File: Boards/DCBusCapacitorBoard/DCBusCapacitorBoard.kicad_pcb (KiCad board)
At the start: 4 copper layers, 89 x 85 mm, 16 parts

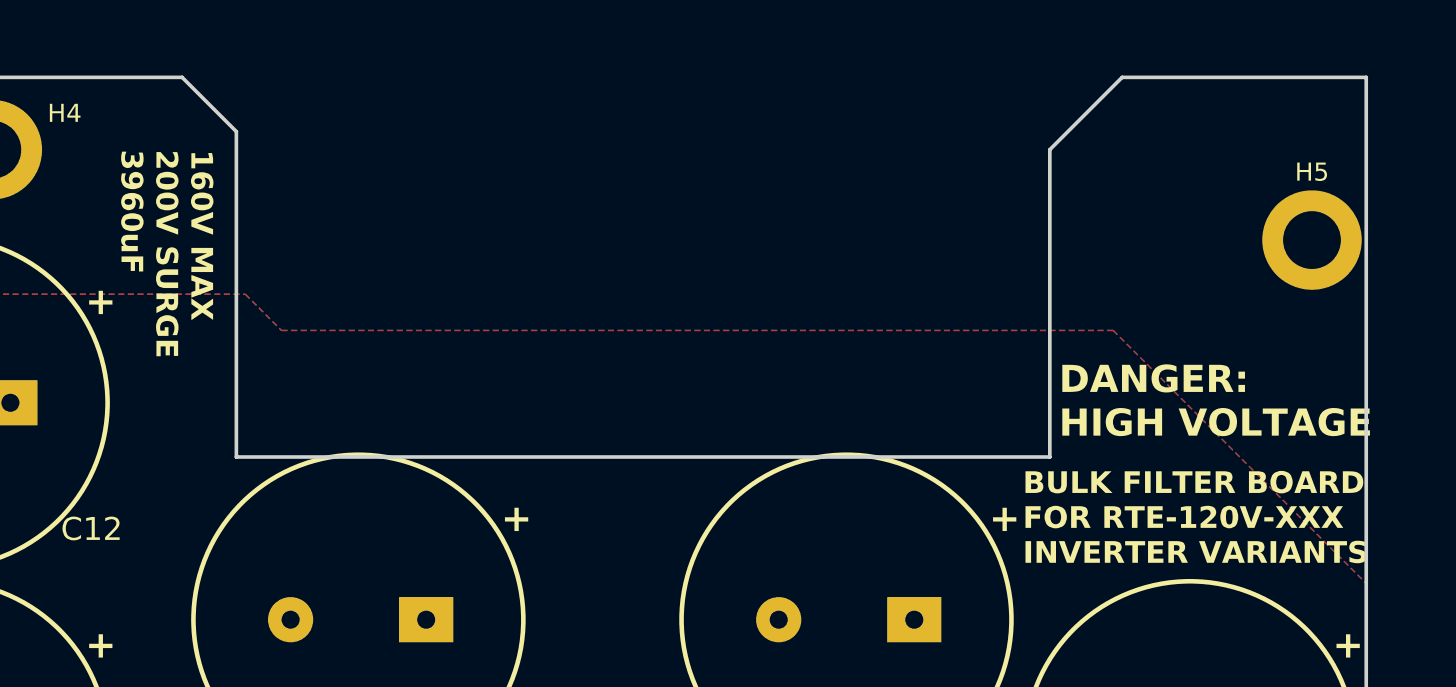
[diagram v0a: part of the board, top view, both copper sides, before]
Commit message: Update Silscreen for variants, fix gate driver and remove todo
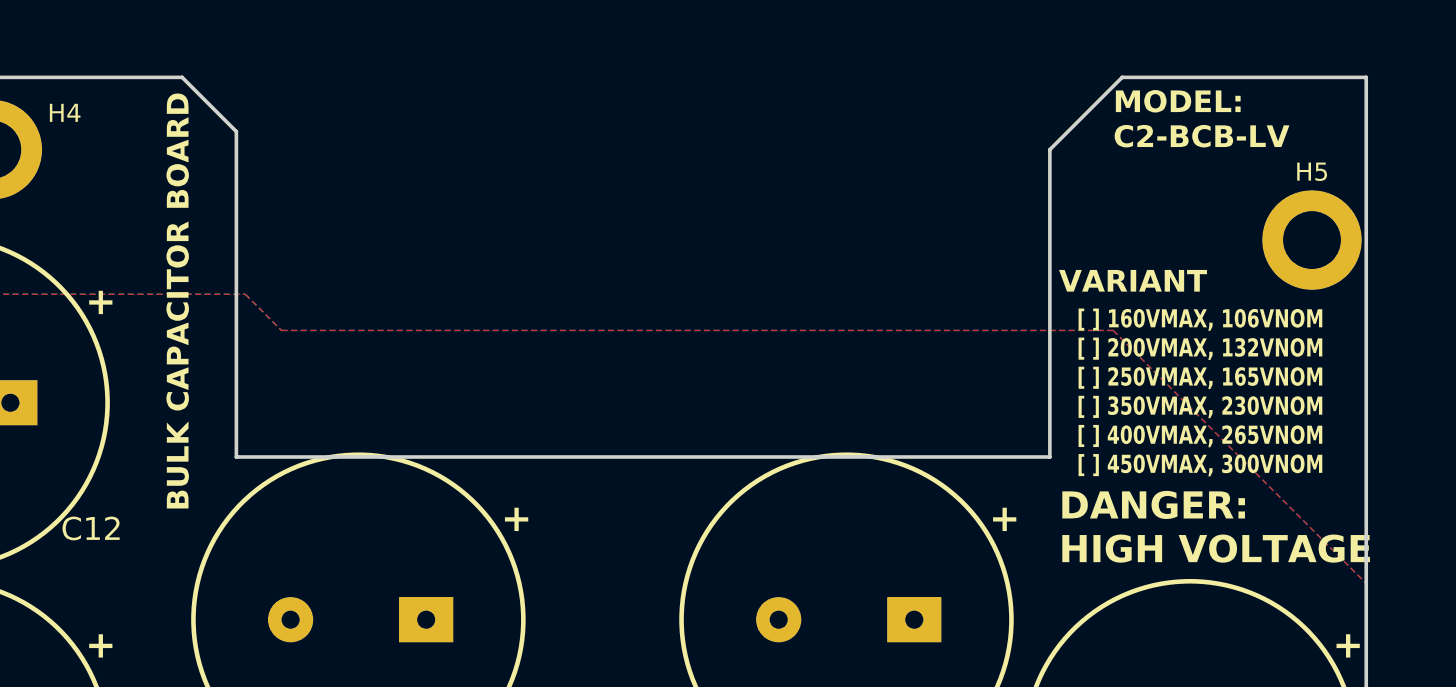
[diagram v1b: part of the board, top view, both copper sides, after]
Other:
- board text added: "BULK CAPACITOR BOARD"
- board text added: "MODEL: C2-BCB-LV"
- board text added: "SERIAL NUMBER"
- board text added: "VARIANT"
- board text added: "[ ] 160VMAX, 106VNOM [ ] 200VMAX, 132VNOM [ ] 250VMAX, 165VNOM [ ] 350VMAX, 230VNOM [ ] 400VMAX, 265VNOM [ ] 450VMAX, 300VNOM"
- board text removed: "160V MAX 200V SURGE 3960uF"
- board text removed: "BULK FILTER BOARD FOR RTE-120V-XXX INVERTER VARIANTS"
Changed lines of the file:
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@@
 			(outputformat 1)
 			(mirror no)
-			(drillshape 1)
+			(drillshape 0)
 			(scaleselection 1)
-			(outputdirectory "")
+			(outputdirectory "Fab/")
 		)
 	)
@@
 		(embedded_fonts no)
 	)
+	(gr_rect
+		(start 74 2)
+		(end 84 12)
+		(stroke
+			(width 0.2)
+			(type solid)
+		)
+		(fill yes)
+		(layer "B.SilkS")
+	)
 	(gr_poly
 		(pts
@@
 		(fill no)
 		(layer "Edge.Cuts")
+	)
+	(gr_text "VARIANT"
+		(at 73 3 0)
+		(layer "F.SilkS")
+		(effects
+			(font
+				(size 1.2 1.2)
+				(thickness 0.225)
+				(bold yes)
+			)
+			(justify left bottom)
+		)
 	)
 	(gr_text "DC LINK +"
@@
 		)
 	)
-	(gr_text "BULK FILTER BOARD\nFOR RTE-120V-XXX\nINVERTER VARIANTS"
-		(at 71 18 0)
+	(gr_text "[ ] 160VMAX, 106VNOM\n[ ] 200VMAX, 132VNOM\n[ ] 250VMAX, 165VNOM\n[ ] 350VMAX, 230VNOM\n[ ] 400VMAX, 265VNOM\n[ ] 450VMAX, 300VNOM"
+		(at 74 13 0)
+		(layer "F.SilkS")
+		(effects
+			(font
+				(size 1 0.75)
+				(thickness 0.1875)
+				(bold yes)
+			)
+			(justify left bottom)
+		)
+	)
+	(gr_text "MODEL:\nC2-BCB-LV\n"
+		(at 76 -5 0)
 		(layer "F.SilkS")
 		(effects
@@
 	)
 	(gr_text "DANGER:\nHIGH VOLTAGE"
-		(at 73 11 0)
+		(at 73 18 0)
 		(layer "F.SilkS" knockout)
 		(effects
@@
 		)
 	)
-	(gr_text "160V MAX\n200V SURGE\n3960uF"
-		(at 21 -5 270)
+	(gr_text "BULK CAPACITOR BOARD"
+		(at 25 15 90)
 		(layer "F.SilkS")
 		(effects
@@
 		)
 	)
+	(gr_text "SERIAL NUMBER"
+		(at 86 15 0)
+		(layer "B.SilkS")
+		(effects
+			(font
+				(size 1.2 1.2)
+				(thickness 0.225)
+				(bold yes)
+			)
+			(justify left bottom mirror)
+		)
+	)
